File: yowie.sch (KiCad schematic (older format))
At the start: 52 parts

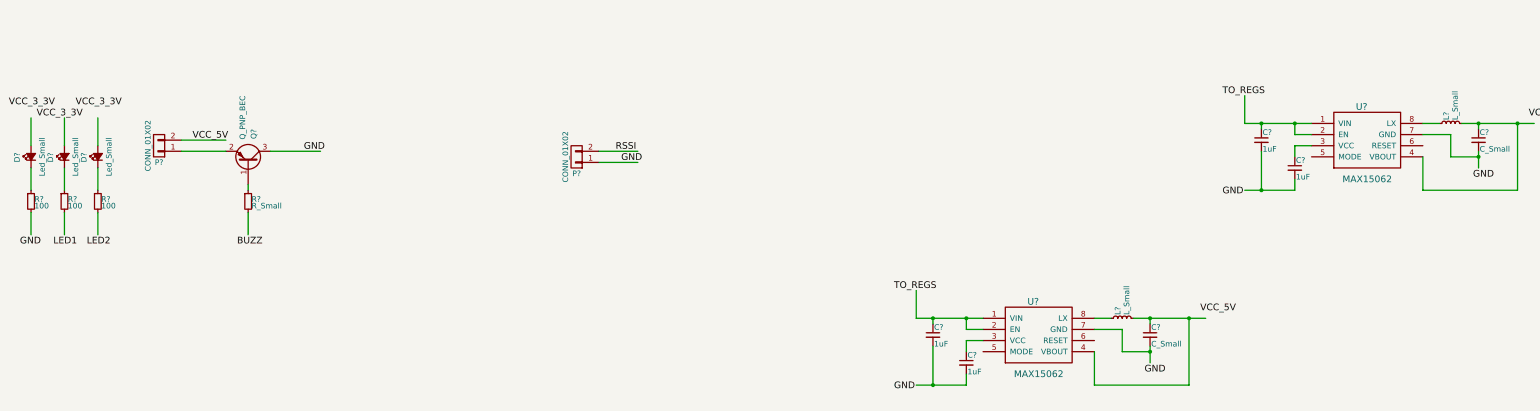
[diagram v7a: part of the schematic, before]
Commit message: Added LM2575
Also edited inductor values for 3.3V and 5V regs
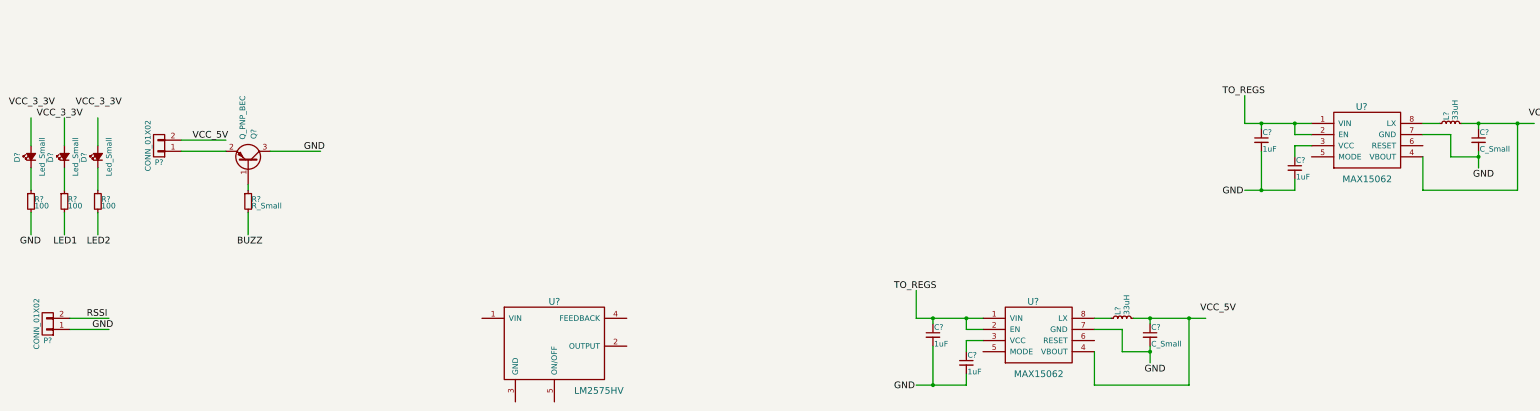
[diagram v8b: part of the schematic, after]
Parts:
- added U?: LM2575HV, symbol LM2575HV
- L? (x2): value L_Small -> 33uH
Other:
- moved on the sheet: P?
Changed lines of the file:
@@
 L CONN_01X02 P?
 U 1 1 56606140
-P 5750 6800
-F 0 "P?" H 5750 6950 50  0000 C CNN
-F 1 "CONN_01X02" V 5850 6800 50  0000 C CNN
-F 2 "" H 5750 6800 60  0000 C CNN
-F 3 "" H 5750 6800 60  0000 C CNN
-	1    5750 6800
+P 1000 8300
+F 0 "P?" H 1000 8450 50  0000 C CNN
+F 1 "CONN_01X02" V 1100 8300 50  0000 C CNN
+F 2 "" H 1000 8300 60  0000 C CNN
+F 3 "" H 1000 8300 60  0000 C CNN
+	1    1000 8300
 	-1   0    0    1
 $EndComp
-Text Label 6100 6750 0    60   ~ 0
+Text Label 1350 8250 0    60   ~ 0
 RSSI
-Text Label 6150 6850 0    60   ~ 0
+Text Label 1400 8350 0    60   ~ 0
 GND
 $Comp
@@
 P 13600 6500
 F 0 "L?" H 13630 6540 50  0000 L CNN
-F 1 "L_Small" H 13630 6460 50  0000 L CNN
+F 1 "33uH" H 13630 6460 50  0000 L CNN
 F 2 "" H 13600 6500 60  0000 C CNN
 F 3 "" H 13600 6500 60  0000 C CNN
@@
 P 10650 8250
 F 0 "L?" H 10680 8290 50  0000 L CNN
-F 1 "L_Small" H 10680 8210 50  0000 L CNN
+F 1 "33uH" H 10680 8210 50  0000 L CNN
 F 2 "" H 10650 8250 60  0000 C CNN
 F 3 "" H 10650 8250 60  0000 C CNN
@@
 	13100 4850 13450 4850
 Wire Wire Line
-	5950 6750 6300 6750
-Wire Wire Line
-	5950 6850 6300 6850
+	1200 8250 1550 8250
+Wire Wire Line
+	1200 8350 1550 8350
 Wire Wire Line
 	11750 6500 12350 6500
@@
 	1100 3650 1350 3650
 Connection ~ 1100 3550
+$Comp
+L LM2575HV U?
+U 1 1 56698559
+P 5400 8000
+F 0 "U?" H 5550 7900 60  0000 C CNN
+F 1 "LM2575HV" H 5950 7100 60  0000 C CNN
+F 2 "" H 5400 8000 60  0000 C CNN
+F 3 "" H 5400 8000 60  0000 C CNN
+	1    5400 8000
+	1    0    0    -1
+$EndComp
 $EndSCHEMATC
